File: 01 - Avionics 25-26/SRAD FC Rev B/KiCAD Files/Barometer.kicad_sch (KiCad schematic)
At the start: 0 parts

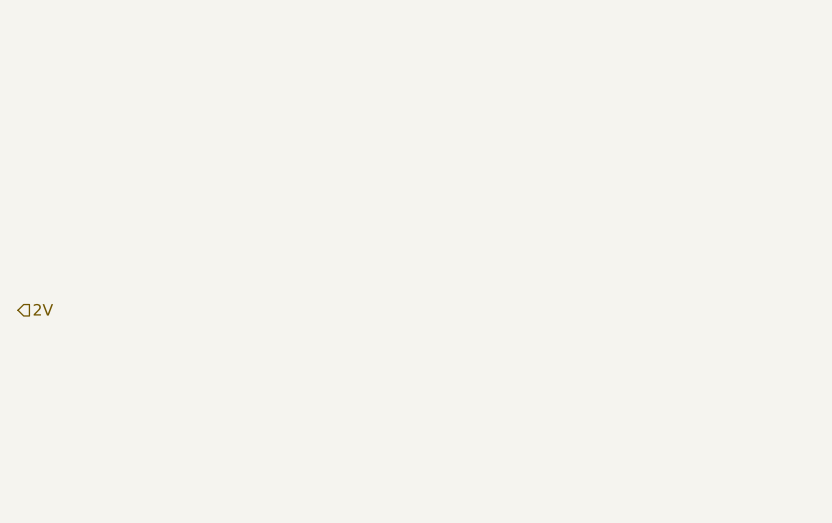
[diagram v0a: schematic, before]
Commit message: Added IMU and Barometer Circuits w/Root Symbols
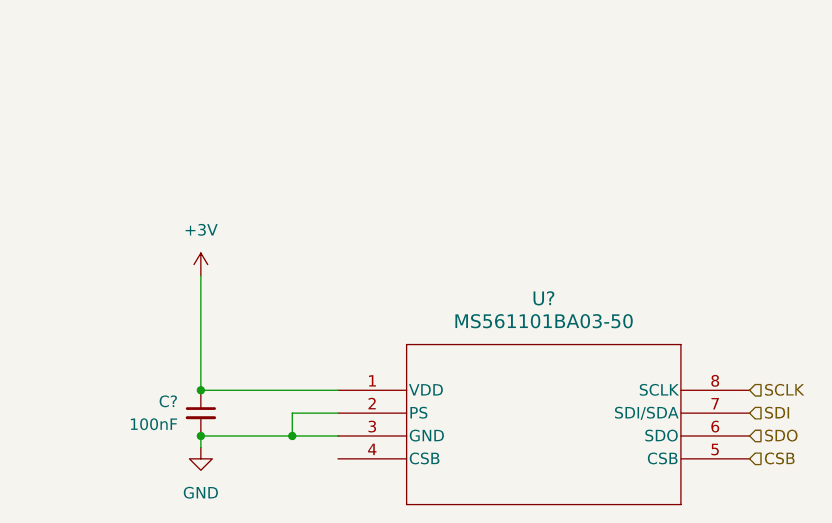
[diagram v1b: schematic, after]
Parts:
- added C?: 100nF, symbol Device:C_Small
- added U?: MS561101BA03-50, SON8_MS5611_TEC, symbol 2025-11-01_19-50-27:MS561101BA03-50
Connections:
- new net +3V: C?.1, U?.1 (VDD)
- new net CSB: U?.5 (CSB)
- new net GND: C?.2, U?.2 (PS), U?.3 (GND)
- new net SCLK: U?.8 (SCLK)
- new net SDI: U?.7 (SDI/SDA)
- new net SDO: U?.6 (SDO)
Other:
- company: (none) -> Missouri S&T Rocket Design Team
- title: (none) -> Barometer (MS5611)

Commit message: added power as hierarchical sheet pins
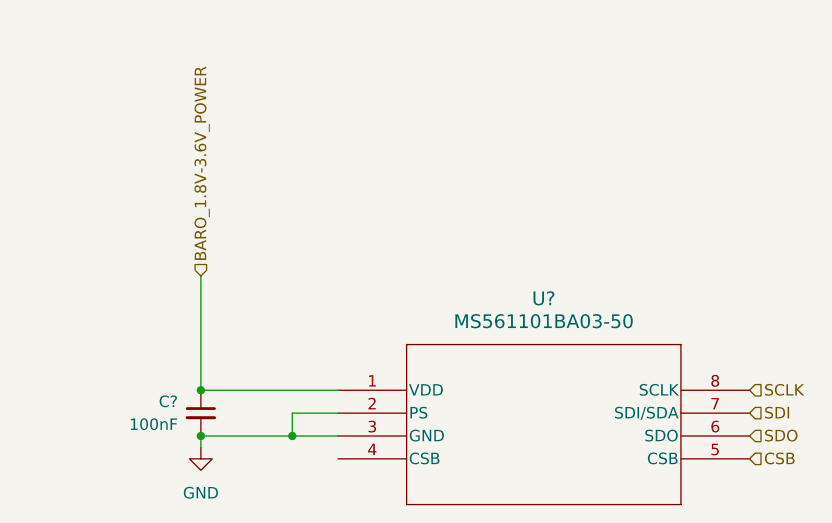
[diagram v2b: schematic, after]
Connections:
- net +3V renamed BARO_1.8V-3.6V_POWER
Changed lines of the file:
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@@
+		)
+	)
+	(hierarchical_label "BARO_1.8V-3.6V_POWER"
+		(shape input)
+		(at 90.17 69.85 90)
+		(effects
+			(font
+				(size 1.27 1.27)
+			)
+			(justify left)
 		)
 	)
@@
 					(unit 1)
 				)
-			)
-		)
-	)
-	(symbol
-		(lib_id "power:+3V0")
-		(at 90.17 69.85 0)
-		(unit 1)
-		(exclude_from_sim no)
-		(in_bom yes)
-		(on_board yes)
-		(dnp no)
-		(property "Reference" "#PWR?"
-			(at 90.17 73.66 0)
-			(effects
-				(font
-					(size 1.27 1.27)
-				)
-				(hide yes)
-			)
-		)
-		(property "Value" "+3V"
-			(at 90.17 64.77 0)
-			(effects
-				(font
-					(size 1.27 1.27)
-				)
-			)
-		)
-		(property "Footprint" ""
-			(at 90.17 69.85 0)
-			(effects
-				(font
-					(size 1.27 1.27)
-				)
-				(hide yes)
-			)
-		)
-		(property "Datasheet" ""
-			(at 90.17 69.85 0)
-			(effects
-				(font
-					(size 1.27 1.27)
-				)
-				(hide yes)
-			)
-		)
-		(property "Description" "Power symbol creates a global label with name \"+3V0\""
-			(at 90.17 69.85 0)
-			(effects
-				(font
-					(size 1.27 1.27)
-				)
-				(hide yes)
-			)
-		)
-		(pin "1"
-		)
-		(instances
-			(project "SRAD FC Rev B"
-				(path "/1dd9e63a-24f2-43c6-ae21-66b89e6998f2/ed116dc3-f59f-469d-b0da-086663032b42"
-					(reference "#PWR?")
-					(unit 1)
-				)
-			)
-			(project ""
-				(path "/93a562d5-048c-4bb1-bff7-151c85a6af71"
-					(reference "#PWR01")
-					(unit 1)
-				)

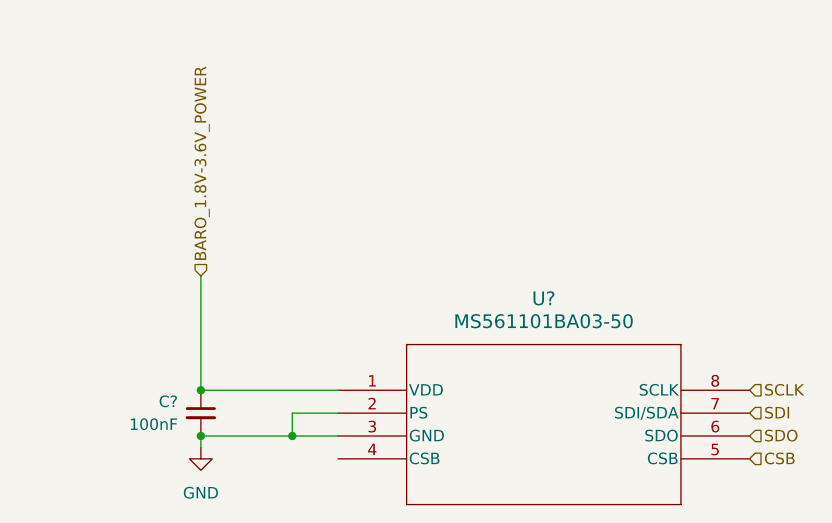
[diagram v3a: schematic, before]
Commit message: general fixes for sheet sheet, ERC error fixes
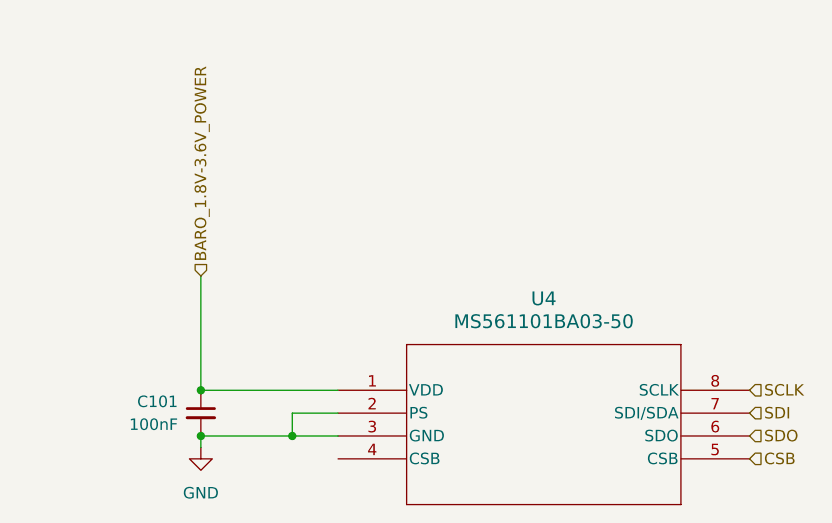
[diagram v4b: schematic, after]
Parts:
- gave numbers to parts that had none: 2
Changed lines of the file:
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@@
 		(dnp no)
 		(fields_autoplaced yes)
-		(property "Reference" "U?"
+		(property "Reference" "U4"
 			(at 128.27 72.39 0)
 			(effects
@@
 			(project "SRAD FC Rev B"
 				(path "/1dd9e63a-24f2-43c6-ae21-66b89e6998f2/ed116dc3-f59f-469d-b0da-086663032b42"
-					(reference "U?")
+					(reference "U4")
 					(unit 1)
 				)
@@
 		(on_board yes)
 		(dnp no)
-		(property "Reference" "C?"
+		(property "Reference" "C101"
 			(at 87.63 83.8262 0)
 			(effects
@@
 			(project "SRAD FC Rev B"
 				(path "/1dd9e63a-24f2-43c6-ae21-66b89e6998f2/ed116dc3-f59f-469d-b0da-086663032b42"
-					(reference "C?")
+					(reference "C101")
 					(unit 1)
 				)
